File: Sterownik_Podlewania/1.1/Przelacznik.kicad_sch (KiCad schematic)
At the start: 6 parts, among them SW1 SW_Nidec_CAS-120A1, SW2 SW_Nidec_CAS-120A1

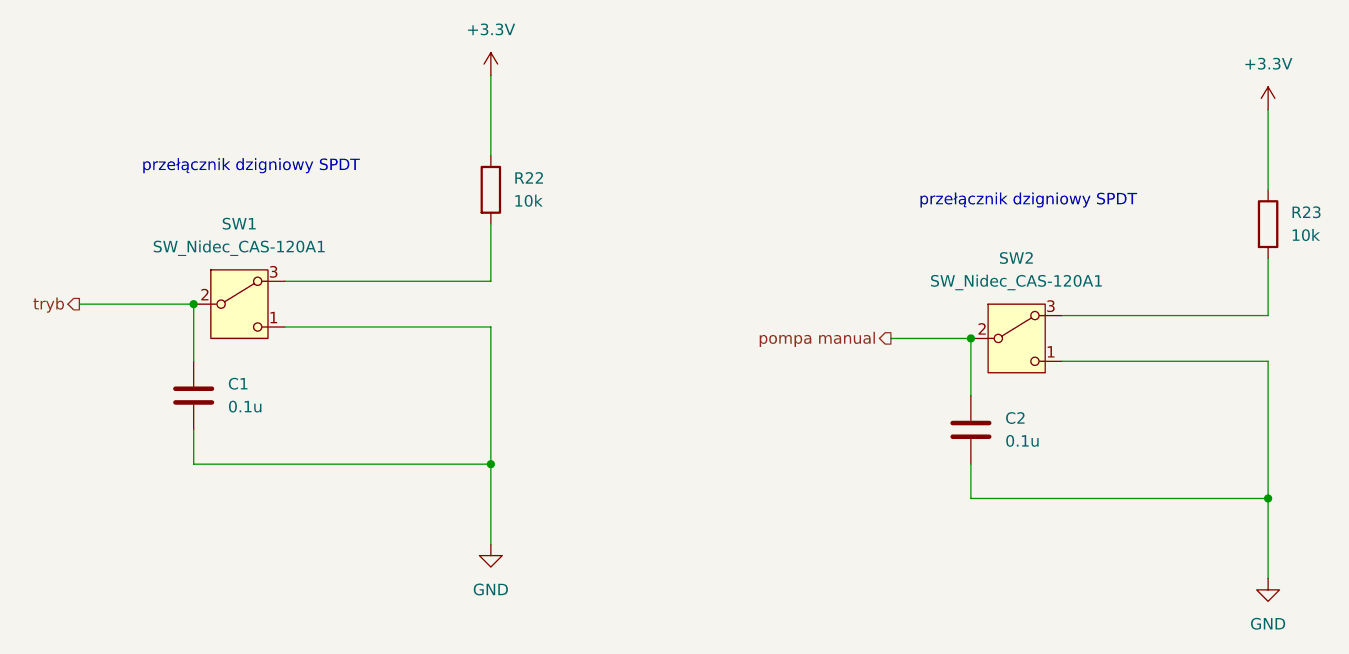
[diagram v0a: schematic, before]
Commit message: Poprawiono błędy połączeń SDA,SCL, dodno drugą magistralę I2C, pociągnięcie nowych ścieżek
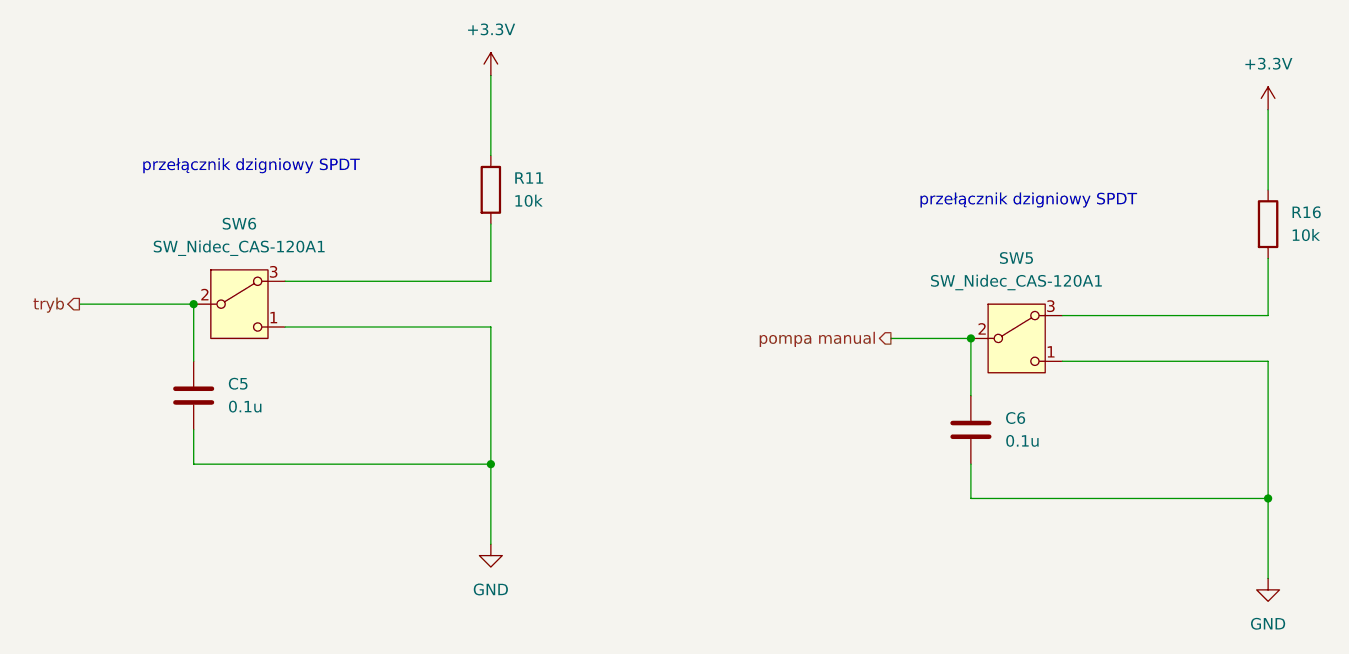
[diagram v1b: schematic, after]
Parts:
- renumbered C1 to C5, C2 to C6, R22 to R11, R23 to R16, SW2 to SW5, SW1 to SW6
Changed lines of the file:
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@@
 		(dnp no)
 		(fields_autoplaced yes)
-		(property "Reference" "R23"
+		(property "Reference" "R16"
 			(at 207.01 77.4699 0)
 			(effects
@@
 			(project "Sterownik_Podlewania V1.1"
 				(path "/a66bdf1f-0e2a-4cc5-beb1-605f2a3b9885/f74fd688-52b9-454a-a8a2-9357f9e49f57"
-					(reference "R23")
+					(reference "R16")
 					(unit 1)
 				)
@@
 		(dnp no)
 		(fields_autoplaced yes)
-		(property "Reference" "R22"
+		(property "Reference" "R11"
 			(at 120.65 73.6599 0)
 			(effects
@@
 			(project "Sterownik_Podlewania"
 				(path "/a66bdf1f-0e2a-4cc5-beb1-605f2a3b9885/f74fd688-52b9-454a-a8a2-9357f9e49f57"
-					(reference "R22")
+					(reference "R11")
 					(unit 1)
 				)
@@
 		(dnp no)
 		(fields_autoplaced yes)
-		(property "Reference" "C1"
+		(property "Reference" "C5"
 			(at 88.9 96.5199 0)
 			(effects
@@
 			(project "Sterownik_Podlewania"
 				(path "/a66bdf1f-0e2a-4cc5-beb1-605f2a3b9885/f74fd688-52b9-454a-a8a2-9357f9e49f57"
-					(reference "C1")
+					(reference "C5")
 					(unit 1)
 				)
@@
 		(dnp no)
 		(fields_autoplaced yes)
-		(property "Reference" "C2"
+		(property "Reference" "C6"
 			(at 175.26 100.3299 0)
 			(effects
@@
 			(project "Sterownik_Podlewania V1.1"
 				(path "/a66bdf1f-0e2a-4cc5-beb1-605f2a3b9885/f74fd688-52b9-454a-a8a2-9357f9e49f57"
-					(reference "C2")
+					(reference "C6")
 					(unit 1)
 				)
@@
 		(dnp no)
 		(fields_autoplaced yes)
-		(property "Reference" "SW1"
+		(property "Reference" "SW6"
 			(at 90.17 78.74 0)
 			(effects
@@
 			(project "Sterownik_Podlewania"
 				(path "/a66bdf1f-0e2a-4cc5-beb1-605f2a3b9885/f74fd688-52b9-454a-a8a2-9357f9e49f57"
-					(reference "SW1")
+					(reference "SW6")
 					(unit 1)
 				)
@@
 		(dnp no)
 		(fields_autoplaced yes)
-		(property "Reference" "SW2"
+		(property "Reference" "SW5"
 			(at 176.53 82.55 0)
 			(effects
@@
 			(project "Sterownik_Podlewania V1.1"
 				(path "/a66bdf1f-0e2a-4cc5-beb1-605f2a3b9885/f74fd688-52b9-454a-a8a2-9357f9e49f57"
-					(reference "SW2")
-					(unit 1)
-				)
+					(reference "SW5")
+					(unit 1)
+				)

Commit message: Usunięcie zewnętrzego zasilania 12 i stabilizatora napięcia, korekcja zasilania wzmacniacz operacyjny moduł zasilania
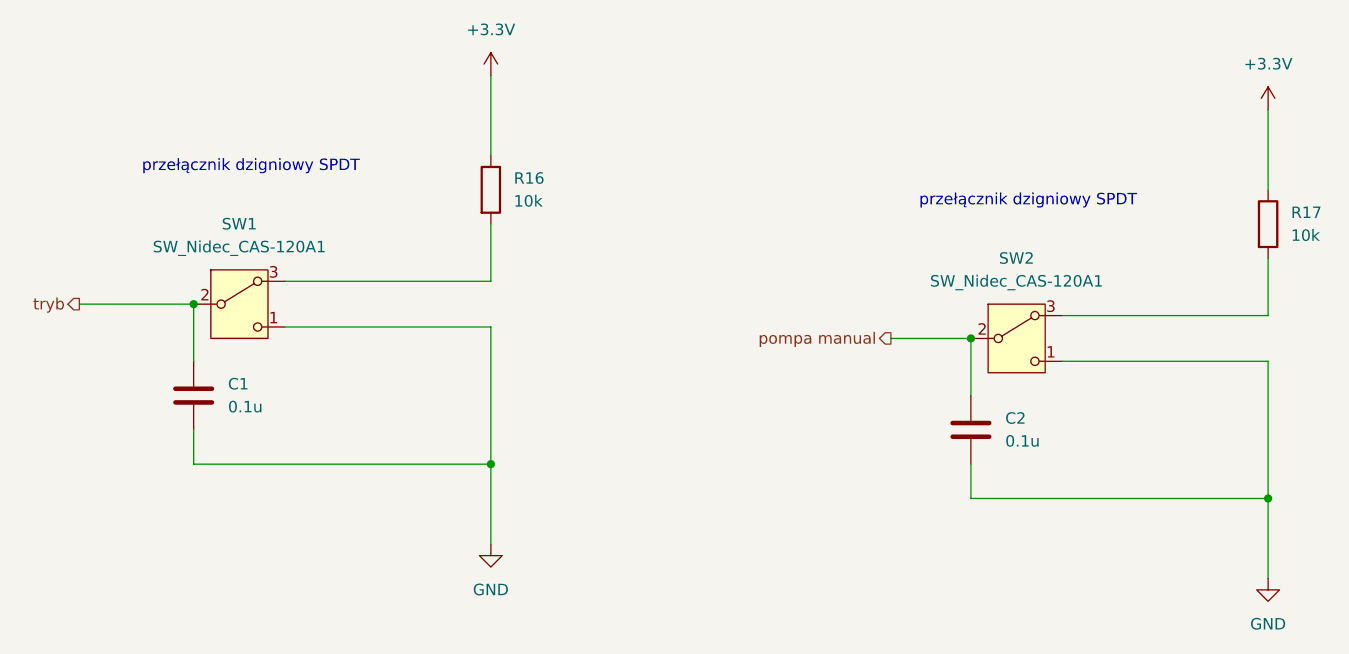
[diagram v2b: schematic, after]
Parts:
- renumbered C5 to C1, C6 to C2, R11 to R16, R16 to R17, SW6 to SW1, SW5 to SW2
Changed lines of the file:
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@@
 		(dnp no)
 		(fields_autoplaced yes)
-		(property "Reference" "#PWR06"
+		(property "Reference" "#PWR064"
 			(at 204.47 69.85 0)
 			(effects
@@
 			(project "Sterownik_Podlewania V1.1"
 				(path "/a66bdf1f-0e2a-4cc5-beb1-605f2a3b9885/f74fd688-52b9-454a-a8a2-9357f9e49f57"
-					(reference "#PWR06")
+					(reference "#PWR064")
 					(unit 1)
 				)
@@
 		(dnp no)
 		(fields_autoplaced yes)
-		(property "Reference" "R16"
+		(property "Reference" "R17"
 			(at 207.01 77.4699 0)
 			(effects
@@
 			(project "Sterownik_Podlewania V1.1"
 				(path "/a66bdf1f-0e2a-4cc5-beb1-605f2a3b9885/f74fd688-52b9-454a-a8a2-9357f9e49f57"
-					(reference "R16")
+					(reference "R17")
 					(unit 1)
 				)
@@
 		(dnp no)
 		(fields_autoplaced yes)
-		(property "Reference" "R11"
+		(property "Reference" "R16"
 			(at 120.65 73.6599 0)
 			(effects
@@
 			(project "Sterownik_Podlewania"
 				(path "/a66bdf1f-0e2a-4cc5-beb1-605f2a3b9885/f74fd688-52b9-454a-a8a2-9357f9e49f57"
-					(reference "R11")
+					(reference "R16")
 					(unit 1)
 				)
@@
 		(dnp no)
 		(fields_autoplaced yes)
-		(property "Reference" "#PWR057"
+		(property "Reference" "#PWR063"
 			(at 118.11 120.65 0)
 			(effects
@@
 			(project "Sterownik_Podlewania"
 				(path "/a66bdf1f-0e2a-4cc5-beb1-605f2a3b9885/f74fd688-52b9-454a-a8a2-9357f9e49f57"
-					(reference "#PWR057")
+					(reference "#PWR063")
 					(unit 1)
 				)
@@
 		(dnp no)
 		(fields_autoplaced yes)
-		(property "Reference" "C5"
+		(property "Reference" "C1"
 			(at 88.9 96.5199 0)
 			(effects
@@
 			(project "Sterownik_Podlewania"
 				(path "/a66bdf1f-0e2a-4cc5-beb1-605f2a3b9885/f74fd688-52b9-454a-a8a2-9357f9e49f57"
-					(reference "C5")
+					(reference "C1")
 					(unit 1)
 				)
@@
 		(dnp no)
 		(fields_autoplaced yes)
-		(property "Reference" "C6"
+		(property "Reference" "C2"
 			(at 175.26 100.3299 0)
 			(effects
@@
 			(project "Sterownik_Podlewania V1.1"
 				(path "/a66bdf1f-0e2a-4cc5-beb1-605f2a3b9885/f74fd688-52b9-454a-a8a2-9357f9e49f57"
-					(reference "C6")
+					(reference "C2")
 					(unit 1)
 				)
@@
 		(dnp no)
 		(fields_autoplaced yes)
-		(property "Reference" "#PWR08"
+		(property "Reference" "#PWR065"
 			(at 204.47 124.46 0)
 			(effects
@@
 			(project "Sterownik_Podlewania V1.1"
 				(path "/a66bdf1f-0e2a-4cc5-beb1-605f2a3b9885/f74fd688-52b9-454a-a8a2-9357f9e49f57"
-					(reference "#PWR08")
+					(reference "#PWR065")
 					(unit 1)
 				)
@@
 		(dnp no)
 		(fields_autoplaced yes)
-		(property "Reference" "#PWR056"
+		(property "Reference" "#PWR062"
 			(at 118.11 66.04 0)
 			(effects
@@
 			(project "Sterownik_Podlewania"
 				(path "/a66bdf1f-0e2a-4cc5-beb1-605f2a3b9885/f74fd688-52b9-454a-a8a2-9357f9e49f57"
-					(reference "#PWR056")
+					(reference "#PWR062")
 					(unit 1)
 				)
@@
 		(dnp no)
 		(fields_autoplaced yes)
-		(property "Reference" "SW6"
+		(property "Reference" "SW1"
 			(at 90.17 78.74 0)
 			(effects
@@
 			(project "Sterownik_Podlewania"
 				(path "/a66bdf1f-0e2a-4cc5-beb1-605f2a3b9885/f74fd688-52b9-454a-a8a2-9357f9e49f57"
-					(reference "SW6")
+					(reference "SW1")
 					(unit 1)
 				)
@@
 		(dnp no)
 		(fields_autoplaced yes)
-		(property "Reference" "SW5"
+		(property "Reference" "SW2"
 			(at 176.53 82.55 0)
 			(effects
@@
 			(project "Sterownik_Podlewania V1.1"
 				(path "/a66bdf1f-0e2a-4cc5-beb1-605f2a3b9885/f74fd688-52b9-454a-a8a2-9357f9e49f57"
-					(reference "SW5")
-					(unit 1)
-				)
+					(reference "SW2")
+					(unit 1)
+				)

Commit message: Werja plików podesłana Mariuszkowi, dodane opisy i numeracja poprawna dla steronwika, w module poprawniono opis złącze ethernet
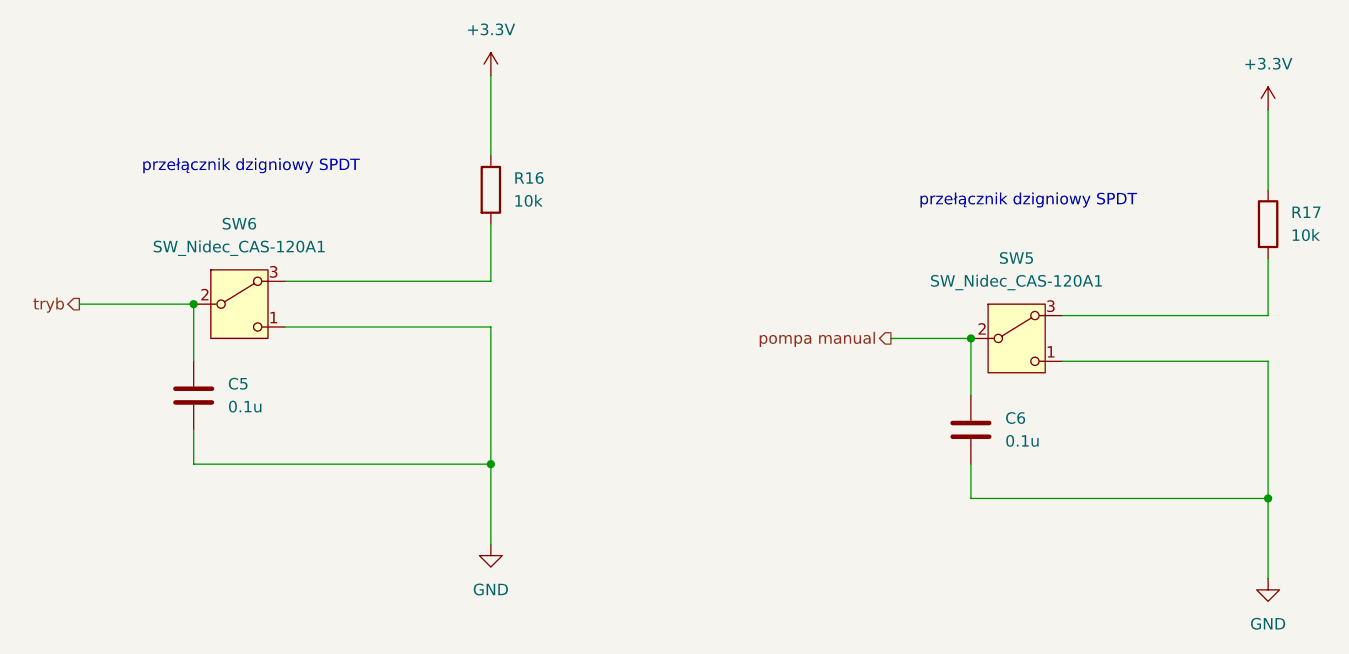
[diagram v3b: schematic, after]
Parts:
- renumbered C1 to C5, C2 to C6, SW2 to SW5, SW1 to SW6
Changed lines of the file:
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@@
 		(dnp no)
 		(fields_autoplaced yes)
-		(property "Reference" "C1"
+		(property "Reference" "C5"
 			(at 88.9 96.5199 0)
 			(effects
@@
 			(project "Sterownik_Podlewania"
 				(path "/a66bdf1f-0e2a-4cc5-beb1-605f2a3b9885/f74fd688-52b9-454a-a8a2-9357f9e49f57"
-					(reference "C1")
+					(reference "C5")
 					(unit 1)
 				)
@@
 		(dnp no)
 		(fields_autoplaced yes)
-		(property "Reference" "C2"
+		(property "Reference" "C6"
 			(at 175.26 100.3299 0)
 			(effects
@@
 			(project "Sterownik_Podlewania V1.1"
 				(path "/a66bdf1f-0e2a-4cc5-beb1-605f2a3b9885/f74fd688-52b9-454a-a8a2-9357f9e49f57"
-					(reference "C2")
+					(reference "C6")
 					(unit 1)
 				)
@@
 		(dnp no)
 		(fields_autoplaced yes)
-		(property "Reference" "SW1"
+		(property "Reference" "SW6"
 			(at 90.17 78.74 0)
 			(effects
@@
 			(project "Sterownik_Podlewania"
 				(path "/a66bdf1f-0e2a-4cc5-beb1-605f2a3b9885/f74fd688-52b9-454a-a8a2-9357f9e49f57"
-					(reference "SW1")
+					(reference "SW6")
 					(unit 1)
 				)
@@
 		(dnp no)
 		(fields_autoplaced yes)
-		(property "Reference" "SW2"
+		(property "Reference" "SW5"
 			(at 176.53 82.55 0)
 			(effects
@@
 			(project "Sterownik_Podlewania V1.1"
 				(path "/a66bdf1f-0e2a-4cc5-beb1-605f2a3b9885/f74fd688-52b9-454a-a8a2-9357f9e49f57"
-					(reference "SW2")
-					(unit 1)
-				)
+					(reference "SW5")
+					(unit 1)
+				)
